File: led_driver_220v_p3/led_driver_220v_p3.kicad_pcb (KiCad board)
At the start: 2 copper layers, 100 x 100 mm, 98 parts, among them CN1 3.3V, J1 LED Chain, J1 SWD, J10 DC-Output-5V, J10 IO3, J11 DC-Output-230V, J13 D, J14 V, J2 DEBUG, J2 I2C2_Pmod, J3 I2C2_Qwiic, J3 RUN, J4 DC_DC, J4 SPI2_Pmod, J5 GPIO_Pmod, J5 OLED_I2C, J6 RUN, J6 USART1_Pmod, J7 I2S_Pmod, J7 IO1, J8 DEBUG, J8 Input_5V, J9 AC-Input-230V, J9 IO2, P1 USB_C_Plug_USB2.0, P2 USB_C_Plug_USB2.0, Q1 BSS138, SW1 RESET, U1 E28-2G4M27S-MY, U1 TLV75533PDBV, U2 ESP32-WROOM-32-MY, U2 STM32G030F6, U3 SPX3819M5-L, X1 0.1uF

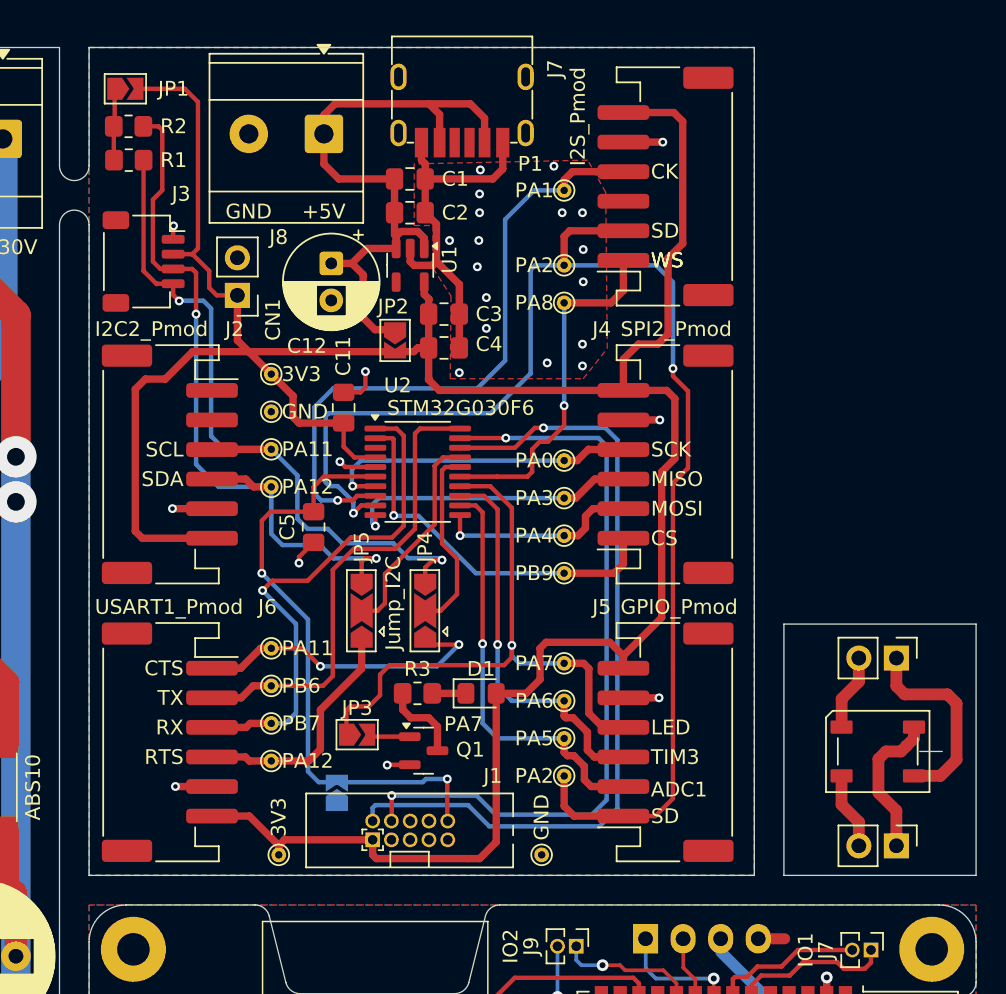
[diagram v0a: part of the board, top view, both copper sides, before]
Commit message: led_driver_220v_p3 update
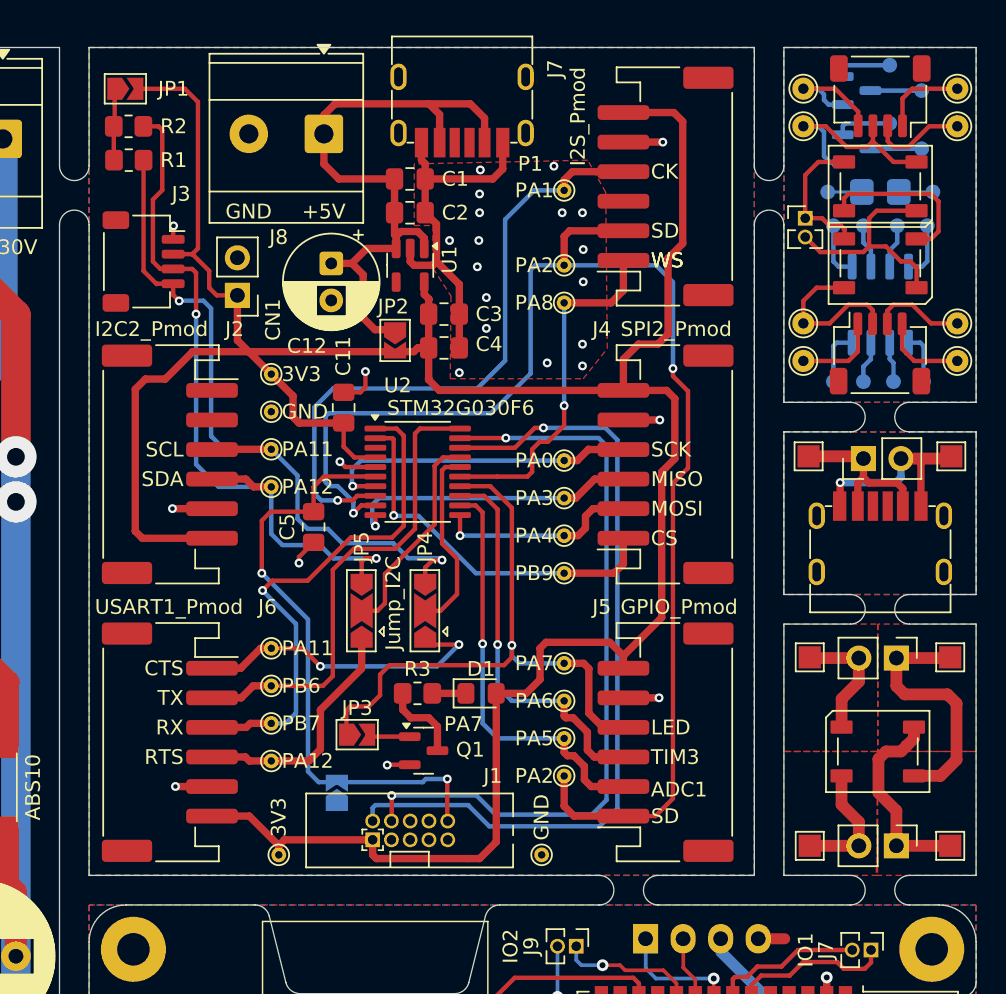
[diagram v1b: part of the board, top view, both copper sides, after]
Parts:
- added D4: WS2812B, LED_SMD:LED_WS2812B_PLCC4_5.0x5.0mm_P3.2mm, F.Cu at (143.5, 49.4)
- added D5: WS2812B, LED_SMD:LED_WS2812B_PLCC4_5.0x5.0mm_P3.2mm, F.Cu at (143.5, 54.6)
- added J12: V, Connector_PinHeader_2.54mm:PinHeader_1x02_P2.54mm_Vertical, F.Cu at (142.4, 67.8)
- added J15: Qwiic_IN, Connector_JST:JST_SH_SM04B-SRSS-TB_1x04-1MP_P1.00mm_Horizontal, F.Cu at (143.5, 43.3)
- added J16: Qwiic_Out, Connector_JST:JST_SH_SM04B-SRSS-TB_1x04-1MP_P1.00mm_Horizontal, F.Cu at (143.5, 60.7)
- added J17: 5.0V, Connector_PinHeader_1.27mm:PinHeader_1x02_P1.27mm_Vertical, F.Cu at (138.4, 51.5)
- added J51: SOIC-8, Package_SO:SO-8_3.9x4.9mm_P1.27mm, B.Cu at (143.5, 57.4)
- added P3: USB_C_Plug_USB2.0, zhaw:USB_C_DEALON_009, F.Cu at (143.5, 71.4)
- added Q2: BSS138, Package_TO_SOT_SMD:SOT-23, B.Cu at (141.9, 42.9)
- added Q3: BSS138, Package_TO_SOT_SMD:SOT-23, B.Cu at (141.9, 46.9)
- added R4: R, Resistor_SMD:R_1206_3216Metric_Pad1.30x1.75mm_HandSolder, B.Cu at (143.5, 49.8)
- added TP16: USB+5V, TestPoint:TestPoint_Pad_1.5x1.5mm, F.Cu at (138.7, 67.7)
- added TP17: USB-GND, TestPoint:TestPoint_Pad_1.5x1.5mm, F.Cu at (148.3, 67.7)
- added TP18: USB+5V, TestPoint:TestPoint_Pad_1.5x1.5mm, F.Cu at (148.2, 81.2)
- added TP19: USB-GND, TestPoint:TestPoint_Pad_1.5x1.5mm, F.Cu at (138.8, 81.2)
- added TP20: USB+5V, TestPoint:TestPoint_Pad_1.5x1.5mm, F.Cu at (148.2, 94.0)
- added TP21: USB-GND, TestPoint:TestPoint_Pad_1.5x1.5mm, F.Cu at (138.8, 94.0)
- added TP22: ~, TestPoint:TestPoint_THTPad_D1.5mm_Drill0.7mm, F.Cu at (138.3, 42.8)
- added TP23: ~, TestPoint:TestPoint_THTPad_D1.5mm_Drill0.7mm, F.Cu at (138.3, 45.3)
- added TP24: ~, TestPoint:TestPoint_THTPad_D1.5mm_Drill0.7mm, F.Cu at (148.7, 58.7)
- added TP25: ~, TestPoint:TestPoint_THTPad_D1.5mm_Drill0.7mm, F.Cu at (148.7, 42.8)
- added TP26: ~, TestPoint:TestPoint_THTPad_D1.5mm_Drill0.7mm, F.Cu at (138.3, 61.2)
- added TP27: ~, TestPoint:TestPoint_THTPad_D1.5mm_Drill0.7mm, F.Cu at (138.3, 58.7)
- added TP28: ~, TestPoint:TestPoint_THTPad_D1.5mm_Drill0.7mm, F.Cu at (148.7, 45.3)
- added TP29: ~, TestPoint:TestPoint_THTPad_D1.5mm_Drill0.7mm, F.Cu at (148.7, 61.2)
- added TP30: ~, TestPoint:TestPoint_Pad_D1.0mm, B.Cu at (146.3, 42.9)
- added TP31: ~, TestPoint:TestPoint_Pad_D1.0mm, B.Cu at (146.3, 46.9)
- added TP32: ~, TestPoint:TestPoint_Pad_D1.0mm, B.Cu at (144.2, 45.1)
- added TP33: ~, TestPoint:TestPoint_Pad_D1.0mm, B.Cu at (144.2, 41.2)
- added TP34: ~, TestPoint:TestPoint_Pad_D1.0mm, B.Cu at (146.7, 52.1)
- added TP35: ~, TestPoint:TestPoint_Pad_D1.0mm, B.Cu at (144.7, 52.1)
- added TP36: ~, TestPoint:TestPoint_Pad_D1.0mm, B.Cu at (142.4, 52.1)
- added TP37: ~, TestPoint:TestPoint_Pad_D1.0mm, B.Cu at (140.3, 52.1)
- added TP38: ~, TestPoint:TestPoint_Pad_D1.0mm, B.Cu at (146.4, 62.6)
- added TP39: ~, TestPoint:TestPoint_Pad_D1.0mm, B.Cu at (144.4, 62.6)
- added TP40: ~, TestPoint:TestPoint_Pad_D1.0mm, B.Cu at (142.4, 62.6)
- added TP41: ~, TestPoint:TestPoint_Pad_D1.0mm, B.Cu at (140.3, 62.6)
- added TP42: ~, TestPoint:TestPoint_Pad_D1.0mm, B.Cu at (147.1, 49.8)
- added TP43: ~, TestPoint:TestPoint_Pad_D1.0mm, B.Cu at (140.0, 49.8)
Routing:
- net /Addition/Q_GND: track 0.00 -> 27.0 mm
- net /Addition/USB-GND: track 0.00 -> 15.7 mm, vias 0 -> 1
- net /Addition/Q_SDA_IN: track 0.00 -> 14.7 mm
- net /Addition/Q_3.3V: track 0.00 -> 12.8 mm
- net /Addition/USB+5V: track 0.00 -> 12.0 mm
- net Net-(D4-DOUT): track 0.00 -> 11.3 mm
- net /Addition/Q_SDA_OUT: track 0.00 -> 10.9 mm
- net /Addition/Q_5.0V: track 0.00 -> 9.99 mm
- net /Addition/Q_SCL_IN: track 0.00 -> 8.64 mm
- net /Addition/Q_SCL_OUT: track 0.00 -> 5.82 mm
- net Net-(Q3-S): track 0.00 -> 3.83 mm
- net Net-(Q2-S): track 0.00 -> 3.83 mm
- net Net-(J51-Pin_4): track 0.00 -> 3.83 mm
- net Net-(J51-Pin_1): track 0.00 -> 3.83 mm
- net Net-(J51-Pin_8): track 0.00 -> 3.77 mm
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- added copper zone on F.Cu, net +5V
- added copper zone on F.Cu, net /Addition/IN
- added copper zone on F.Cu, net /Addition/OUT
- added copper zone on F.Cu, net /Addition/Q_3.3V
- added copper zone on B.Cu, net /Addition/Q_GND
- added copper zone on F.Cu, net /Addition/USB+5V
- added copper zone on B.Cu, net /Addition/USB-GND
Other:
- outline, holes or cut-outs redrawn

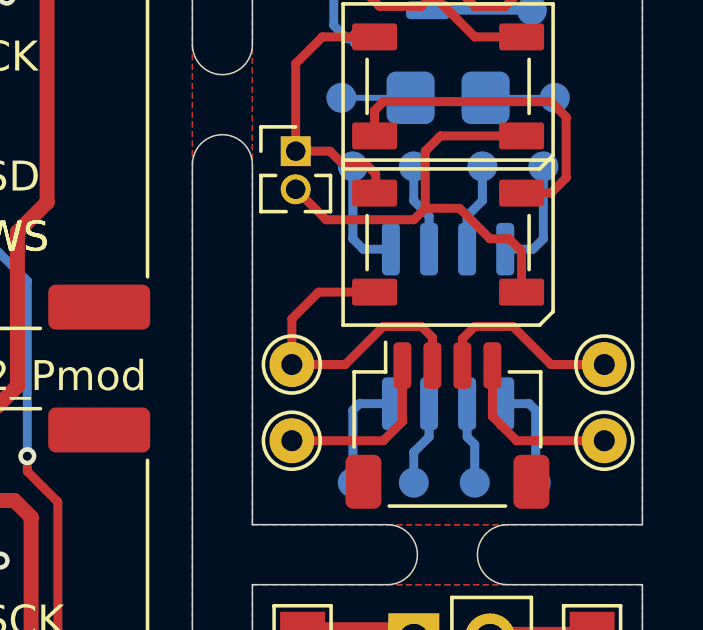
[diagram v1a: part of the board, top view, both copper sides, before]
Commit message: led_driver_220v_p3 update
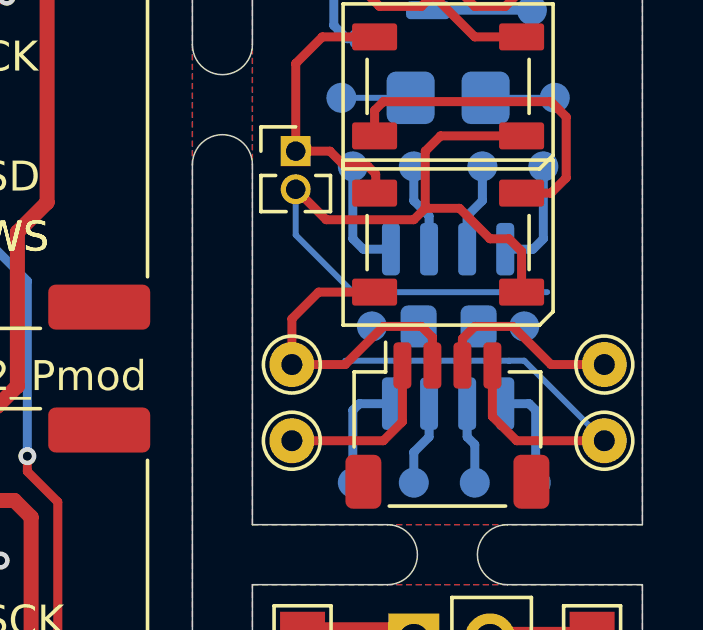
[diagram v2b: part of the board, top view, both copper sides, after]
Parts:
- added R5: R, Resistor_SMD:R_0805_2012Metric_Pad1.20x1.40mm_HandSolder, B.Cu at (143.5, 57.4)
- added TP44: ~, TestPoint:TestPoint_Pad_D1.0mm, B.Cu at (146.1, 57.4)
- added TP45: ~, TestPoint:TestPoint_Pad_D1.0mm, B.Cu at (141.0, 57.4)
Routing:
- net /Addition/Q_GND: track 27.0 -> 47.4 mm
- net Net-(R5-Pad2): track 0.00 -> 1.56 mm
- net Net-(R5-Pad1): track 0.00 -> 1.52 mm

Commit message: led_driver_220v_p3 update + gerber
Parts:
- added R6: 56k, Resistor_SMD:R_0805_2012Metric_Pad1.20x1.40mm_HandSolder, B.Cu at (143.2, 89.4)
- added R7: 22k, Resistor_SMD:R_0805_2012Metric_Pad1.20x1.40mm_HandSolder, B.Cu at (147.0, 89.4)
- added R8: R, Resistor_SMD:R_1206_3216Metric_Pad1.30x1.75mm_HandSolder, B.Cu at (139.1, 87.1)
- added R9: R, Resistor_SMD:R_0805_2012Metric_Pad1.20x1.40mm_HandSolder, B.Cu at (147.7, 83.8)
- added TP46: ~, TestPoint:TestPoint_Pad_D1.0mm, B.Cu at (139.1, 83.6)
- added TP47: ~, TestPoint:TestPoint_Pad_D1.0mm, B.Cu at (147.7, 80.8)
- added TP48: ~, TestPoint:TestPoint_Pad_D1.0mm, B.Cu at (139.1, 90.7)
- added TP49: ~, TestPoint:TestPoint_Pad_D1.0mm, B.Cu at (147.7, 86.9)
- added U3: SPX3819M5-L, Package_TO_SOT_SMD:SOT-23-5, B.Cu at (143.3, 86.0)
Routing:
- net /Addition/OUT: track 13.8 -> 22.7 mm
- net +5V: track 77.8 -> 84.6 mm
- net Net-(U3-ADJ): track 4.27 -> 8.41 mm
- net Net-(R9-Pad1): track 0.00 -> 2.06 mm
- net Net-(R9-Pad2): track 0.00 -> 2.03 mm
- net Net-(R8-Pad2): track 0.00 -> 2.01 mm
- net Net-(R8-Pad1): track 0.00 -> 2.01 mm
